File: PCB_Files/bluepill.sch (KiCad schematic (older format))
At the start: 7 parts, among them J1 TYPE-C-31-M12_13, J2 Conn_01x20_Female, J3 Conn_01x20_Female, J4 Conn_01x06_Female, J5 Conn_01x04_Female, SW1 SW_Push, U1 STM32F103x8_B-LQFP48

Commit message: Further tracing
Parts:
- added C1, C2, C3, C6: 100n, Capacitor_SMD:C_0402_1005Metric, symbol Device:C_Small
- added C4: 1u, Capacitor_SMD:C_0402_1005Metric, symbol Device:C_Small
- added C5: 10u, Capacitor_SMD:C_0402_1005Metric, symbol Device:C_Small
- added D1: D_Schottky_Small, Diode_SMD:D_0603_1608Metric, symbol Device:D_Schottky_Small
- added F1: 0.5A trip, Fuse:Fuse_0603_1608Metric, symbol Device:Fuse_Small
- added Q1: DTC143Z, Package_TO_SOT_SMD:SOT-23, symbol Transistor_BJT:DTC143Z
- added R1, R2: 22R, Resistor_SMD:R_0402_1005Metric, symbol Device:R_Small
- added R3, R4, R7: 100k, Resistor_SMD:R_0402_1005Metric, symbol Device:R_Small
- added R5: 10k, Resistor_SMD:R_0402_1005Metric, symbol Device:R_Small
- added R6: 1R, Resistor_SMD:R_0402_1005Metric, symbol Device:R_Small
- added R8: 1k, Resistor_SMD:R_0402_1005Metric, symbol Device:R_Small
- added U3: TPS709xxDBV, acheron_Components:SOT-23-5, symbol acheronSymbols:TPS709xxDBV
- added U4: USBLC6-2SC6, acheron_Components:SOT-23-6, symbol Power_Protection:USBLC6-2SC6
- U1: footprint acheron_Components:LQFP-48_7x7mm_P0.5mm -> acheron_Components:UQFN-48-1EP_6x6mm_P0.4mm_EP4.62x4.62mm; symbol acheronSymbols:STM32F103x8_B-LQFP48 -> acheronSymbols:STM32F103x8_B-UQFN48
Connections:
- net GND: now also J2.1 (Pin_1), J2.2 (Pin_2), J3.19 (Pin_19), J4.3 (Pin_3), J4.4 (Pin_4), SW1.1, U1.35 (VSS_2), U1.47 (VSS_3), U1.49 (THERMAL), U1.8 (VSSA), C1.2, C2.1, C3.2, C4.2, C5.2, C6.2, D1.2 (A), Q1.2 (E), R7.2, U3.1 (GND), U4.2 (GND); no longer J2.19 (Pin_19), J3.1 (Pin_1), J3.2 (Pin_2)
- net VBAT: now reaches U1.1 (VBAT)
- net VBAT: now also J2.20 (Pin_20)
- net PA0: now reaches U1.10 (PA0/ADC_IN0/WKUP)
- net PA0: now also J2.16 (Pin_16)
- net PA1: now reaches U1.11 (PA1/ADC12_IN1/TIM2_CH3)
- net PA1: now also J2.15 (Pin_15)
- net PA2: now reaches U1.12 (PA2/ADC12_IN2)
- net PA2: now also J2.14 (Pin_14)
- net PA3: now reaches U1.13 (PA3/TIM2_CH4/ADC12_IN3)
- net PA3: now also J2.13 (Pin_13)
- net PA4: now reaches U1.14 (PA4/SPI1_NSS/ADC12_IN4)
- net PA4: now also J2.12 (Pin_12)
- net PA5: now reaches U1.15 (PA5/ADC12_IN5/SPI1_SCK)
- net PA5: now also J2.11 (Pin_11)
- net PA6: now reaches U1.16 (PA6/SPI1_MISO/ADC12_IN6/TIM3_CH1)
- net PA6: now also J2.10 (Pin_10)
- net PA7: now reaches U1.17 (PA7/SPI1_MOSI/ADC12_IN7/TIM3_CH2)
- net PA7: now also J2.9 (Pin_9)
- net PB0: now reaches U1.18 (PB0/TIM3_CH3/ADC12_IN8)
- net PB0: now also J2.8 (Pin_8)
- net PB1: now reaches U1.19 (PB1/TIM3_CH4/ADC12_IN9)
- net PB1: now also J2.7 (Pin_7)
- net PC13: now reaches U1.2 (PC13/TAMPER/RTC)
- net PC13: now also J2.19 (Pin_19)
- net BOOT1: now reaches U1.20 (PB2/BOOT1)
- net BOOT1: now also R3.2
- net PB10: now reaches U1.21 (PB10/I2C2_SCL/USART3_TX)
- net PB10: now also J2.6 (Pin_6)
- net PB11: now reaches U1.22 (PB11/TIM2_CH4/I2C2_SDA/USART3_rX)
- net PB11: now also J2.5 (Pin_5)
- net PB12: now reaches U1.25 (PB12/SPI1_NSS/I2C2_SMBAI/USART3_CK/TIM1_BKIN)
- net PB12: now also J3.1 (Pin_1)
- net PB13: now reaches U1.26 (SPI2_SCK/USART3_CTS/TIM1_CH1N/PB13)
- net PB13: now also J3.2 (Pin_2)
- net PB14: now reaches U1.27 (SPI2_MISO/USART3_RTS/TIM1_CH2N/PB14)
- net PB14: now also J3.3 (Pin_3)
- net PB15: now reaches U1.28 (SPI2_MOSI/TIM1_CH3N/B15)
- net PB15: now also J3.4 (Pin_4)
- net PA8: now reaches U1.29 (USART1_CK/TIM1_CH1/MCO/PA8)
- net PA8: now also J3.5 (Pin_5)
- net PC14: now reaches U1.3 (PC14/OSC32_IN)
- net PC14: now also J2.18 (Pin_18)
- net PA9: now reaches U1.30 (USART1_TX/TIM1_CH2/PA9)
- net PA9: now also J3.6 (Pin_6)
- net PA10: now reaches U1.31 (USART1_RX/TIM1_CH3/PA10)
- net PA10: now also J3.7 (Pin_7)
- net DN: now reaches U1.32 (USB_DM/USART1_CTS/CANRX/TIM1_CH4/PA11)
- net DN: now also U4.1 (IO1)
- net DP: now reaches U1.33 (USART1_RTS/CANTX/USB_DP/TIM1_ETR/PA12)
- net DP: now also U4.3 (IO2)
- net PA13: now reaches U1.34 (SWDIO/PA13)
- net SWCLK: now reaches U1.37 (SWCLK/PA14)
- net PA15: now reaches U1.38 (JTDI/PA15)
- net PA15: now also J3.10 (Pin_10)
- net PB3: now reaches U1.39 (JTDO/PB3)
- net PB3: now also J3.11 (Pin_11)
- net PC15: now reaches U1.4 (PC15/OSC32_OUT)
- net PC15: now also J2.17 (Pin_17)
- net PB4: now reaches U1.40 (JNTRST/PB4)
- net PB4: now also J3.12 (Pin_12)
- net PB5: now reaches U1.41 (I2C1_SMBAI/PB5)
- net PB5: now also J3.13 (Pin_13)
- net PB6: now reaches U1.42 (I2C1_SCL/TIM4_CH1/PB6)
- net PB6: now also J3.14 (Pin_14)
- net PB7: now reaches U1.43 (2C1_SDA/TIM4_CH2/PB7)
- net PB7: now also J3.15 (Pin_15)
- net BOOT0: now reaches U1.44 (BOOT0)
- net BOOT0: now also R4.2
- net PB8: now reaches U1.45 (TIM4_CH3/PB8)
- net PB8: now also J3.16 (Pin_16)
- net PB9: now reaches U1.46 (TIM4_CH4/PB9)
- net PB9: now also J3.17 (Pin_17)
- net RST: now reaches U1.7 (NRST)
- net RST: now also J2.4 (Pin_4), SW1.2, C1.1, R5.2
- net VBUS: now reaches J1.A4 (VBUS)
- net VBUS: now also J1.B4 (VBUS), C6.1, F1.1, U4.5 (VBUS)
- net ConnUSBP: now reaches J1.A6 (D+)
- net ConnUSBP: now also J1.B6 (D+), R2.2
- net ConnUSBN: now reaches J1.A7 (D-)
- net ConnUSBN: now also J1.B7 (D-), R1.2
- net 5V: now reaches J3.18 (Pin_18)
- net 5V: now also C3.1, C5.1, D1.1 (K), F1.2, R7.1, U3.2 (VIN)
- net 3V3: now reaches J3.20 (Pin_20)
- net 3V3: now also J2.3 (Pin_3), J4.1 (Pin_1), J4.6 (Pin_6), C2.2, C4.1, R5.1, R6.2, R8.2, U3.3 (VOUT)
- net PA11: now reaches J3.8 (Pin_8)
- net PA12: now reaches J3.9 (Pin_9)
- net at J4.2 (Pin_2): now also R3.1
- net at J4.5 (Pin_5): now also R4.1
- net JTAG_3V3: now reaches J5.1 (Pin_1)
- net JTAG_3V3: now also Q1.1 (B), R6.1
- net SWD: now reaches J5.2 (Pin_2)
- net SWDIO: now reaches J5.3 (Pin_3)
- new net DBusN: R1.1, U4.6 (IO1)
- new net DBusP: R2.1, U4.4 (IO2)
- new net LDO_EN: Q1.3 (C), R8.1, U3.5 (EN)
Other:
- moved on the sheet: J2, J3, J4, J5, SW1

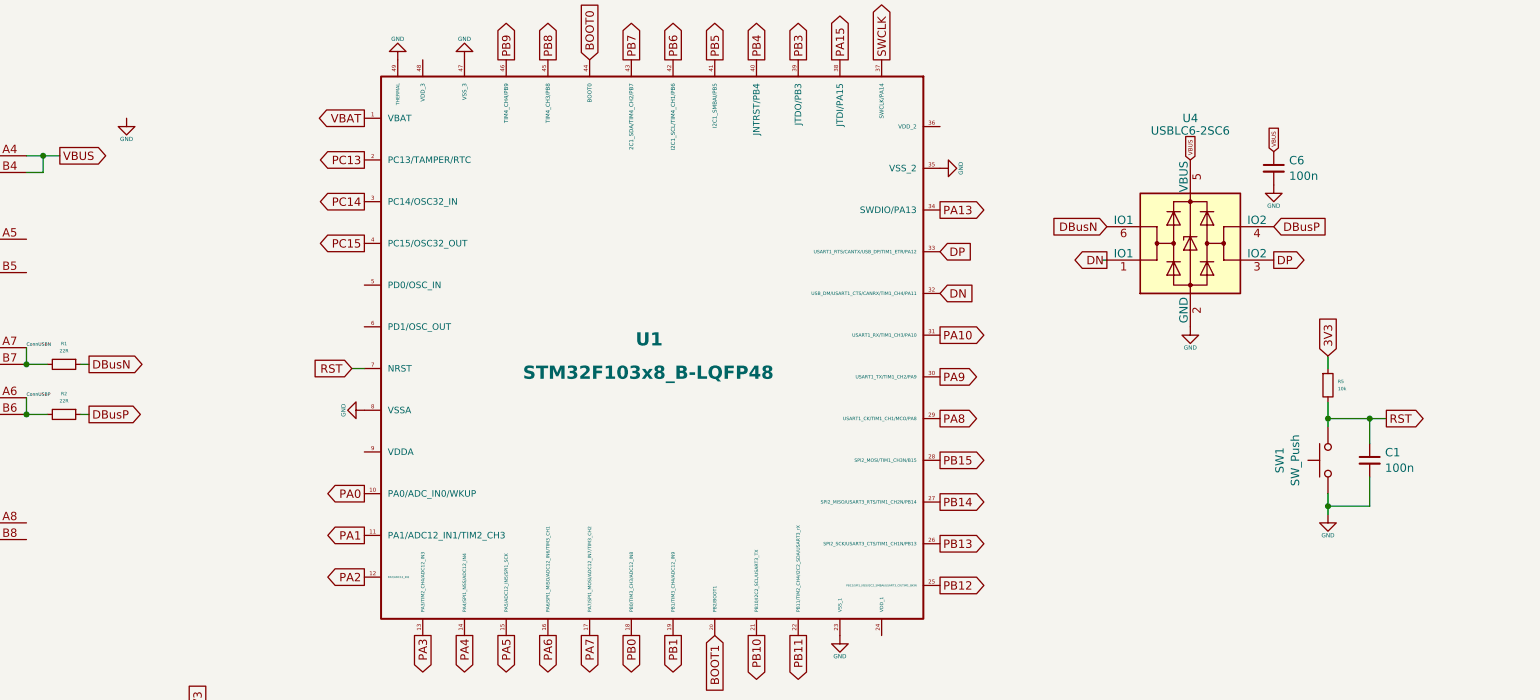
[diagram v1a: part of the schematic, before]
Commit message: Added series resistor in reset net
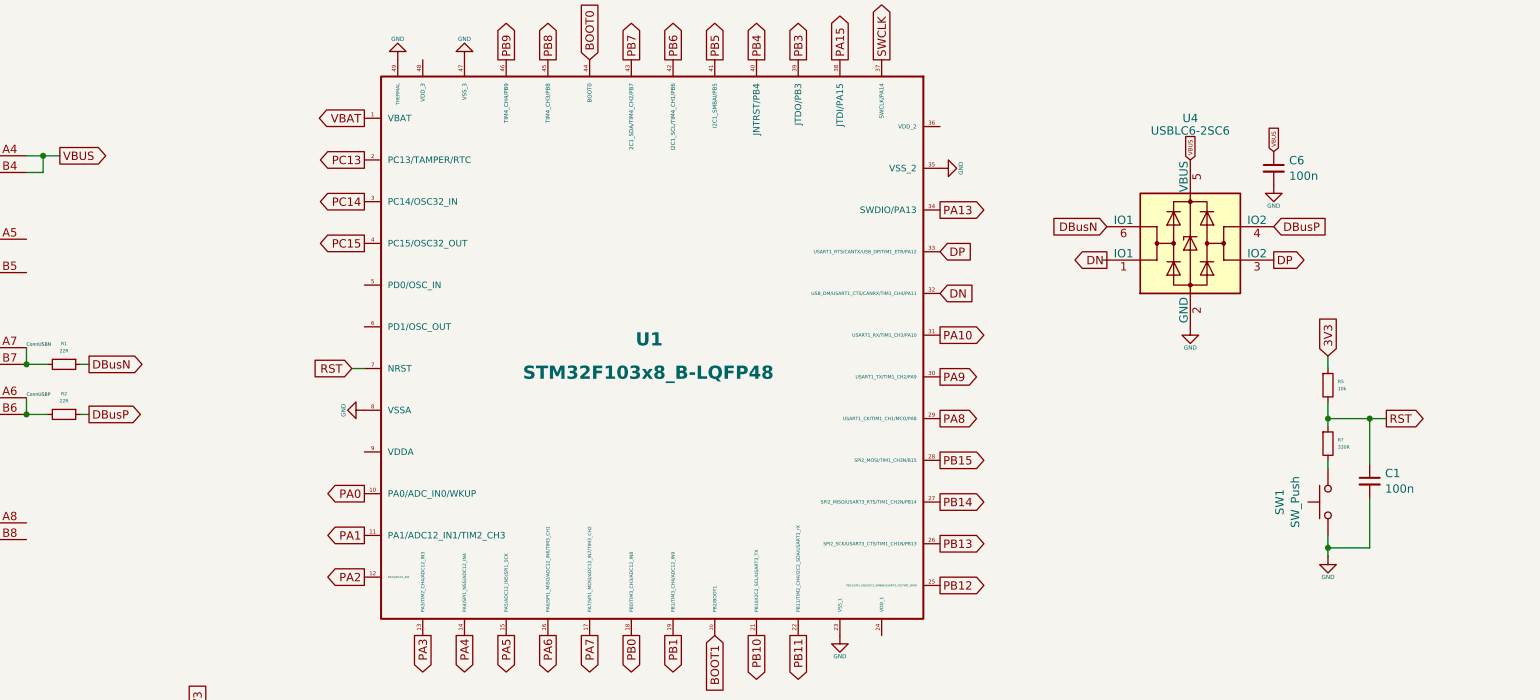
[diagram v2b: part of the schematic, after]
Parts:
- added R?: 330R, Resistor_SMD:R_0402_1005Metric, symbol Device:R_Small
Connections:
- net RST: now also R?.1; no longer SW1.2
- new net: R?.2, SW1.2
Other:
- moved on the sheet: C1, SW1
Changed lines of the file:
@@
 L Switch:SW_Push SW1
 U 1 1 5D65711A
-P 9975 4500
-F 0 "SW1" H 9975 4789 50  0000 C CNN
-F 1 "SW_Push" H 9975 4696 50  0000 C CNN
-F 2 "acheron_Hardware:smdPushBtn" H 9975 4700 50  0001 C CNN
-F 3 "~" H 9975 4700 50  0001 C CNN
-	1    9975 4500
+P 9975 4750
+F 0 "SW1" H 9975 5039 50  0000 C CNN
+F 1 "SW_Push" H 9975 4946 50  0000 C CNN
+F 2 "acheron_Hardware:smdPushBtn" H 9975 4950 50  0001 C CNN
+F 3 "~" H 9975 4950 50  0001 C CNN
+	1    9975 4750
 	0    -1   -1   0
 $EndComp
@@
 L Device:C_Small C1
 U 1 1 5D65AFD7
-P 10225 4500
-F 0 "C1" H 10317 4547 50  0000 L CNN
-F 1 "100n" H 10317 4454 50  0000 L CNN
-F 2 "Capacitor_SMD:C_0402_1005Metric" H 10225 4500 50  0001 C CNN
-F 3 "~" H 10225 4500 50  0001 C CNN
-	1    10225 4500
+P 10225 4625
+F 0 "C1" H 10317 4672 50  0000 L CNN
+F 1 "100n" H 10317 4579 50  0000 L CNN
+F 2 "Capacitor_SMD:C_0402_1005Metric" H 10225 4625 50  0001 C CNN
+F 3 "~" H 10225 4625 50  0001 C CNN
+	1    10225 4625
 	1    0    0    -1
 $EndComp
@@
 L power:GND #PWR0112
 U 1 1 5D66003F
-P 9975 4825
-F 0 "#PWR0112" H 9975 4575 50  0001 C CNN
-F 1 "GND" H 9975 4700 25  0000 C CNN
-F 2 "" H 9975 4825 50  0001 C CNN
-F 3 "" H 9975 4825 50  0001 C CNN
-	1    9975 4825
-	1    0    0    -1
-$EndComp
-Wire Wire Line
-	9975 4825 9975 4775
+P 9975 5075
+F 0 "#PWR0112" H 9975 4825 50  0001 C CNN
+F 1 "GND" H 9975 4950 25  0000 C CNN
+F 2 "" H 9975 5075 50  0001 C CNN
+F 3 "" H 9975 5075 50  0001 C CNN
+	1    9975 5075
+	1    0    0    -1
+$EndComp
+Wire Wire Line
+	9975 5075 9975 5025
 Wire Wire Line
 	9975 4300 9975 4250
 Wire Wire Line
-	9975 4250 10225 4250
-Wire Wire Line
-	10225 4250 10225 4400
-Wire Wire Line
-	10225 4775 9975 4775
-Wire Wire Line
-	10225 4600 10225 4775
+	10225 5025 9975 5025
 Connection ~ 9975 4250
-Connection ~ 9975 4775
-Wire Wire Line
-	9975 4775 9975 4700
+Connection ~ 9975 5025
+Wire Wire Line
+	9975 5025 9975 4950
 Text GLabel 9975 3875 1    50   Input ~ 0
 3V3
@@
 Text GLabel 5550 2100 1    50   Input ~ 0
 BOOT0
-Wire Wire Line
-	10225 4250 10325 4250
-Connection ~ 10225 4250
 Text GLabel 10325 4250 2    50   Output ~ 0
 RST
@@
 F 3 "~" H 8850 1000 50  0001 C CNN
 	1    8850 1000
-	1    0    0    -1
-$EndComp
-$Comp
-L power:GND #PWR0120
-U 1 1 5D6796B8
-P 2775 2450
-F 0 "#PWR0120" H 2775 2200 50  0001 C CNN
-F 1 "GND" H 2775 2325 25  0000 C CNN
-F 2 "" H 2775 2450 50  0001 C CNN
-F 3 "" H 2775 2450 50  0001 C CNN
-	1    2775 2450
 	1    0    0    -1
 $EndComp
@@
 Text GLabel 5050 2100 1    50   Output ~ 0
 PB9
+$Comp
+L Device:R_Small R?
+U 1 1 5D81BF6C
+P 9975 4400
+F 0 "R?" H 10034 4422 20  0000 L CNN
+F 1 "330R" H 10034 4379 20  0000 L CNN
+F 2 "Resistor_SMD:R_0402_1005Metric" H 9975 4400 50  0001 C CNN
+F 3 "~" H 9975 4400 50  0001 C CNN
+	1    9975 4400
+	1    0    0    -1
+$EndComp
+Wire Wire Line
+	9975 4250 10225 4250
+Connection ~ 10225 4250
+Wire Wire Line
+	10225 4250 10325 4250
+Wire Wire Line
+	9975 4500 9975 4550
+Wire Wire Line
+	10225 4725 10225 5025
+Wire Wire Line
+	10225 4250 10225 4525
 $EndSCHEMATC

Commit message: Further routing
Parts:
- removed Q1: DTC143Z, Package_TO_SOT_SMD:SOT-23, symbol Transistor_BJT:DTC143Z
- removed R8: 1k, Resistor_SMD:R_0402_1005Metric, symbol Device:R_Small
- added C7: 4.7n, Capacitor_SMD:C_0402_1005Metric, symbol Device:C_Small
- added C8, C9: 12p, Capacitor_SMD:C_0402_1005Metric, symbol Device:C_Small
- added RCC1, RCC2: 5.1k, Resistor_SMD:R_0402_1005Metric, symbol Device:R_Small
- added Y1: 16MHz, Crystal:Crystal_SMD_2016-4Pin_2.0x1.6mm, symbol Device:Crystal_GND24
- C2: value 100n -> 1u
- C3: value 100n -> 10u
- F1: value 0.5A trip -> 1.0A trip
- R6: value 1R -> 1M
- U3: symbol acheronSymbols:TPS709xxDBV -> bluepill-rescue:TPS709xxDBV-acheronSymbols
- gave numbers to parts that had none: 1
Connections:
- net LDO_EN is gone; now on net 5V: U3.5 (EN)
- net 3V3: now also J5.1 (Pin_1); no longer R6.2
- net GND: now also R6.2, C7.1, C8.1, C9.2, RCC1.1, RCC2.1, Y1.2, Y1.4
- net at U1.5 (PD0/OSC_IN): now also C8.2, Y1.3
- net at U1.6 (PD1/OSC_OUT): now also C9.1, Y1.1
- net at J1.A5 (CC1): now also RCC1.2
- net at J1.B5 (CC2): now also RCC2.2
- net at J1.S (SHIELD): now also R6.1, C7.2
- removed net JTAG_3V3: J5.1 (Pin_1), R6.1
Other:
- moved on the sheet: C2, J4, R3, R4
